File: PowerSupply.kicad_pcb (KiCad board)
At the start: 2 copper layers, 25 x 12.4 mm, 7 parts, among them P1 USB_OTG, P2 CONN_01X03, U1 LM3671MF-3.3

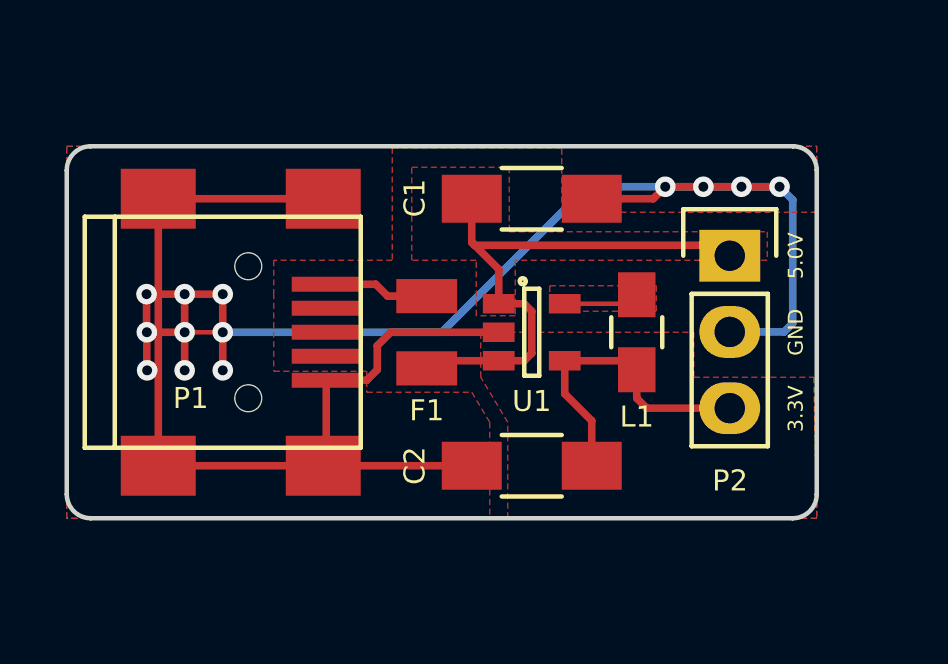
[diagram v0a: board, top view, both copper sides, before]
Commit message: Added MicroSD card adapter
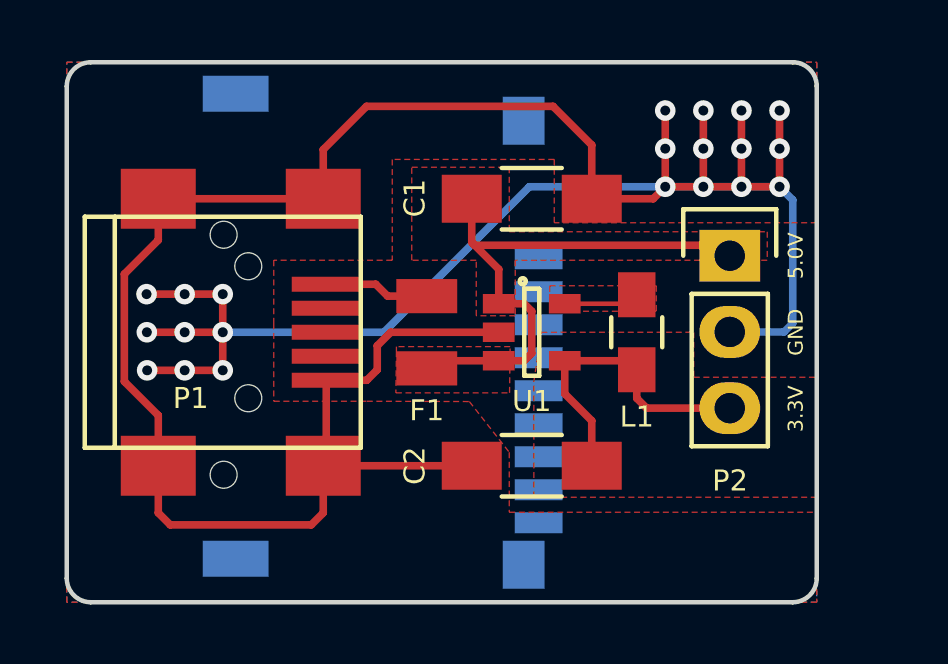
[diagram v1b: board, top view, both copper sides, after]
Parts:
- added U$3: MICRO-SD, PowerSupply:MICRO-SD, B.Cu at (55.2, 156.0)
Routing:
- net GND: track 82.1 -> 106.8 mm, vias 13 -> 21
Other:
- board size 25 x 12.4 mm -> 25 x 18 mm

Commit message: Adds Power-on LED
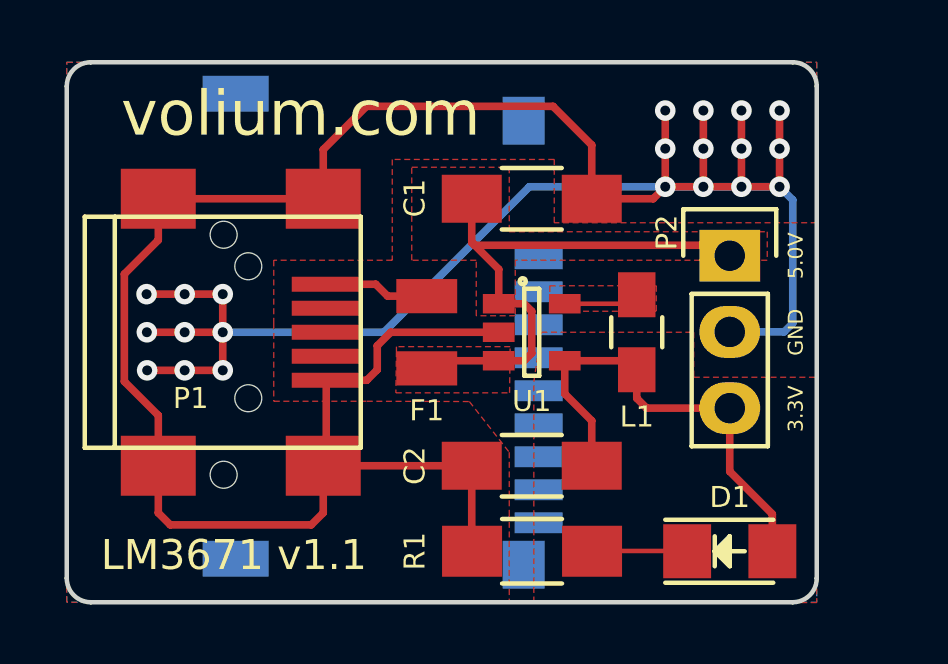
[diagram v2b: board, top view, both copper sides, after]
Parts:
- added D1: LED, LEDs:LED_1206, F.Cu at (72.1, 163.5)
- added R1: R, Resistors_SMD:R_1206_HandSoldering, F.Cu at (65.5, 163.5)
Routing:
- net +3V3: track 10.6 -> 15.9 mm
- net Net-(D1-Pad1): track 0.00 -> 3.17 mm
- net GND: track 106.8 -> 109.7 mm
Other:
- board text added: "LM3671 v1.1"
- board text added: "volium.com"
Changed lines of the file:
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@@
 (kicad_pcb (version 4) (host pcbnew 4.0.3-stable)
   (general
-    (links 17)
+    (links 20)
     (no_connects 0)
     (area 49.924999 147.124999 75.075001 165.275001)
     (thickness 1.6)
-    (drawings 11)
-    (tracks 103)
+    (drawings 13)
+    (tracks 110)
     (zones 0)
-    (modules 8)
-    (nets 9)
+    (modules 10)
+    (nets 10)
   )
   (page A4)
@@
     (0 F.Cu signal)
     (31 B.Cu signal)
-    (34 B.Paste user)
+    (34 B.Paste user hide)
     (35 F.Paste user)
-    (36 B.SilkS user)
+    (36 B.SilkS user hide)
     (37 F.SilkS user)
-    (38 B.Mask user)
+    (38 B.Mask user hide)
     (39 F.Mask user)
     (44 Edge.Cuts user)
@@
   (net 7 "Net-(P1-Pad4)")
   (net 8 "Net-(F1-Pad1)")
+  (net 9 "Net-(D1-Pad1)")
   (net_class Default "This is the default net class."
     (clearance 0.1524)
@@
     (uvia_dia 0.762)
     (uvia_drill 0.508)
+    (add_net "Net-(D1-Pad1)")
     (add_net "Net-(L1-Pad1)")
     (add_net "Net-(P1-Pad2)")
@@
     (descr "Through hole pin header")
     (tags "pin header")
-    (fp_text reference P2 (at 0.01 7.5) (layer F.SilkS)
+    (fp_text reference P2 (at -2.1 -0.78 90) (layer F.SilkS)
       (effects (font (size 0.7 0.7) (thickness 0.15)))
     )
@@
     (pad CD smd rect (at -6.55 10.5 90) (size 0.7 1.6) (layers B.Cu B.Paste B.Mask))
   )
+  (module LEDs:LED_1206 (layer F.Cu)
+    (at 72.1 163.5)
+    (descr "LED 1206 smd package")
+    (tags "LED1206 SMD")
+    (attr smd)
+    (fp_text reference D1 (at 0 -1.8) (layer F.SilkS)
+      (effects (font (size 0.7 0.7) (thickness 0.15)))
+    )
+    (fp_text value LED (at 0 2) (layer F.Fab)
+      (effects (font (size 1 1) (thickness 0.15)))
+    )
+    (fp_line (start -0.5 -0.5) (end -0.5 0.5) (layer F.Fab) (width 0.15))
+    (fp_line (start -0.5 0) (end 0 -0.5) (layer F.Fab) (width 0.15))
+    (fp_line (start 0 0.5) (end -0.5 0) (layer F.Fab) (width 0.15))
+    (fp_line (start 0 -0.5) (end 0 0.5) (layer F.Fab) (width 0.15))
+    (fp_line (start -1.6 0.8) (end -1.6 -0.8) (layer F.Fab) (width 0.15))
+    (fp_line (start 1.6 0.8) (end -1.6 0.8) (layer F.Fab) (width 0.15))
+    (fp_line (start 1.6 -0.8) (end 1.6 0.8) (layer F.Fab) (width 0.15))
+    (fp_line (start -1.6 -0.8) (end 1.6 -0.8) (layer F.Fab) (width 0.15))
+    (fp_line (start -2.15 1.05) (end 1.45 1.05) (layer F.SilkS) (width 0.15))
+    (fp_line (start -2.15 -1.05) (end 1.45 -1.05) (layer F.SilkS) (width 0.15))
+    (fp_line (start -0.1 -0.3) (end -0.1 0.3) (layer F.SilkS) (width 0.15))
+    (fp_line (start -0.1 0.3) (end -0.4 0) (layer F.SilkS) (width 0.15))
+    (fp_line (start -0.4 0) (end -0.2 -0.2) (layer F.SilkS) (width 0.15))
+    (fp_line (start -0.2 -0.2) (end -0.2 0.05) (layer F.SilkS) (width 0.15))
+    (fp_line (start -0.2 0.05) (end -0.25 0) (layer F.SilkS) (width 0.15))
+    (fp_line (start -0.5 -0.5) (end -0.5 0.5) (layer F.SilkS) (width 0.15))
+    (fp_line (start 0 0) (end 0.5 0) (layer F.SilkS) (width 0.15))
+    (fp_line (start -0.5 0) (end 0 -0.5) (layer F.SilkS) (width 0.15))
+    (fp_line (start 0 -0.5) (end 0 0.5) (layer F.SilkS) (width 0.15))
+    (fp_line (start 0 0.5) (end -0.5 0) (layer F.SilkS) (width 0.15))
+    (fp_line (start 2.5 -1.25) (end -2.5 -1.25) (layer F.CrtYd) (width 0.05))
+    (fp_line (start -2.5 -1.25) (end -2.5 1.25) (layer F.CrtYd) (width 0.05))
+    (fp_line (start -2.5 1.25) (end 2.5 1.25) (layer F.CrtYd) (width 0.05))
+    (fp_line (start 2.5 1.25) (end 2.5 -1.25) (layer F.CrtYd) (width 0.05))
+    (pad 2 smd rect (at 1.41986 0 180) (size 1.59766 1.80086) (layers F.Cu F.Paste F.Mask)
+      (net 3 +3V3))
+    (pad 1 smd rect (at -1.41986 0 180) (size 1.59766 1.80086) (layers F.Cu F.Paste F.Mask)
+      (net 9 "Net-(D1-Pad1)"))
+    (model LEDs.3dshapes/LED_1206.wrl
+      (at (xyz 0 0 0))
+      (scale (xyz 1 1 1))
+      (rotate (xyz 0 0 180))
+    )
+  )
+  (module Resistors_SMD:R_1206_HandSoldering (layer F.Cu)
+    (at 65.51 163.5 180)
+    (descr "Resistor SMD 1206, hand soldering")
+    (tags "resistor 1206")
+    (attr smd)
+    (fp_text reference R1 (at 3.91 0 270) (layer F.SilkS)
+      (effects (font (size 0.7 0.7) (thickness 0.15)))
+    )
+    (fp_text value R (at 0 2.3 180) (layer F.Fab)
+      (effects (font (size 1 1) (thickness 0.15)))
+    )
+    (fp_line (start -3.3 -1.2) (end 3.3 -1.2) (layer F.CrtYd) (width 0.05))
+    (fp_line (start -3.3 1.2) (end 3.3 1.2) (layer F.CrtYd) (width 0.05))
+    (fp_line (start -3.3 -1.2) (end -3.3 1.2) (layer F.CrtYd) (width 0.05))
+    (fp_line (start 3.3 -1.2) (end 3.3 1.2) (layer F.CrtYd) (width 0.05))
+    (fp_line (start 1 1.075) (end -1 1.075) (layer F.SilkS) (width 0.15))
+    (fp_line (start -1 -1.075) (end 1 -1.075) (layer F.SilkS) (width 0.15))
+    (pad 1 smd rect (at -2 0 180) (size 2 1.7) (layers F.Cu F.Paste F.Mask)
+      (net 9 "Net-(D1-Pad1)"))
+    (pad 2 smd rect (at 2 0 180) (size 2 1.7) (layers F.Cu F.Paste F.Mask)
+      (net 2 GND))
+    (model Resistors_SMD.3dshapes/R_1206_HandSoldering.wrl
+      (at (xyz 0 0 0))
+      (scale (xyz 1 1 1))
+      (rotate (xyz 0 0 0))
+    )
+  )
+  (gr_text "LM3671 v1.1" (at 55.57 163.63) (layer F.SilkS)
+    (effects (font (size 1 1) (thickness 0.1)))
+  )
+  (gr_text volium.com (at 57.8 148.92) (layer F.SilkS)
+    (effects (font (size 1.5 1.5) (thickness 0.2)))
+  )
   (gr_text 5.0V (at 74.3 153.65 90) (layer F.SilkS)
     (effects (font (size 0.5 0.5) (thickness 0.1)))
@@
   (segment (start 62 157.40396) (end 62.25396 157.15) (width 0.254) (layer F.Cu) (net 1))
   (segment (start 62.25396 157.15) (end 64.4 157.15) (width 0.254) (layer F.Cu) (net 1))
+  (segment (start 63.5 160.65) (end 63.5 163.48) (width 0.254) (layer F.Cu) (net 2))
+  (segment (start 63.5 163.48) (end 63.51 163.49) (width 0.254) (layer F.Cu) (net 2))
   (segment (start 67.5 151.75) (end 67.5 149.96) (width 0.254) (layer F.Cu) (net 2))
   (segment (start 58.55026 150.10974) (end 58.55026 151.74992) (width 0.254) (layer F.Cu) (net 2))
@@
   (segment (start 58.55026 160.65008) (end 63.49992 160.65008) (width 0.254) (layer F.Cu) (net 2))
   (segment (start 63.49992 160.65008) (end 63.5 160.65) (width 0.254) (layer F.Cu) (net 2))
+  (segment (start 73.51986 163.5) (end 73.51986 162.25986) (width 0.254) (layer F.Cu) (net 3) (status 400000))
+  (segment (start 72.1 160.84) (end 72.1 158.73) (width 0.254) (layer F.Cu) (net 3) (status 800000))
+  (segment (start 73.51986 162.25986) (end 72.1 160.84) (width 0.254) (layer F.Cu) (net 3))
   (segment (start 69 157.45) (end 69 158.4) (width 0.254) (layer F.Cu) (net 3))
   (segment (start 69.33 158.73) (end 72.1 158.73) (width 0.254) (layer F.Cu) (net 3))
@@
   (segment (start 60.69604 154.99604) (end 60.2998 154.5998) (width 0.254) (layer F.Cu) (net 8))
   (segment (start 60.2998 154.5998) (end 58.64932 154.5998) (width 0.254) (layer F.Cu) (net 8))
+  (segment (start 67.51 163.49) (end 70.67014 163.49) (width 0.1524) (layer F.Cu) (net 9))
+  (segment (start 70.67014 163.49) (end 70.68014 163.5) (width 0.1524) (layer F.Cu) (net 9))
   (zone (net 3) (net_name +3V3) (layer F.Cu) (hatch edge 0.508)
     (connect_pads (clearance 0.254))
@@
     (polygon
       (pts
-        (xy 70.9 157.7) (xy 75 157.7) (xy 75 161.7) (xy 65.57 161.7) (xy 65.57 157.84)
+        (xy 70.9 157.7) (xy 75 157.7) (xy 75 165.21) (xy 65.57 165.21) (xy 65.57 157.84)
         (xy 65.82 156.2) (xy 70.9 156.2)
       )
@@
         (xy 75 152.55) (xy 74.1 152.55) (xy 66.25 152.55) (xy 66.25 150.44) (xy 60.85 150.44)
         (xy 60.85 153.8) (xy 56.9 153.8) (xy 56.9 155.9) (xy 56.9 158.5) (xy 60 158.5)
-        (xy 63.42 158.51) (xy 64.75 160.2) (xy 64.75 162.2) (xy 75 162.2) (xy 75 165.2)
-        (xy 50 165.2) (xy 50 147.2) (xy 75 147.2)
+        (xy 63.42 158.51) (xy 64.75 160.2) (xy 64.75 162.2) (xy 64.75 165.2) (xy 50 165.2)
+        (xy 50 147.2) (xy 75 147.2)
       )
     )

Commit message: Changes L1 with 1008 package
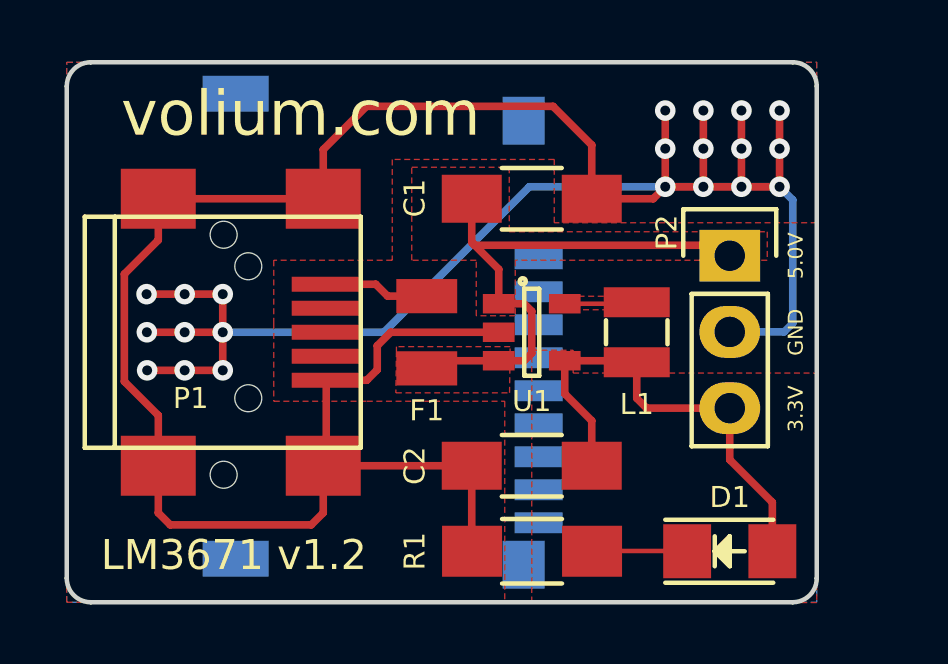
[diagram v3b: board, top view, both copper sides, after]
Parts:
- L1: footprint Capacitors_SMD:C_0805_HandSoldering -> PowerSupply:C_1008_HandSoldering
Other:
- board text added: "LM3671 v1.2"
- board text removed: "LM3671 v1.1"

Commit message: A lot of changes (BOM, layout, routing) Replaces inductor with footprint compatible with CDRH2D09 (Sumida) and NRH2412T (Taiyo Yuden) Removes access to 5V pin (replaced 3-pin connector with 2-pin) Updated layout, now more closely matching Adafruit's version of LM3671 breakout board, and following TI's layout example.
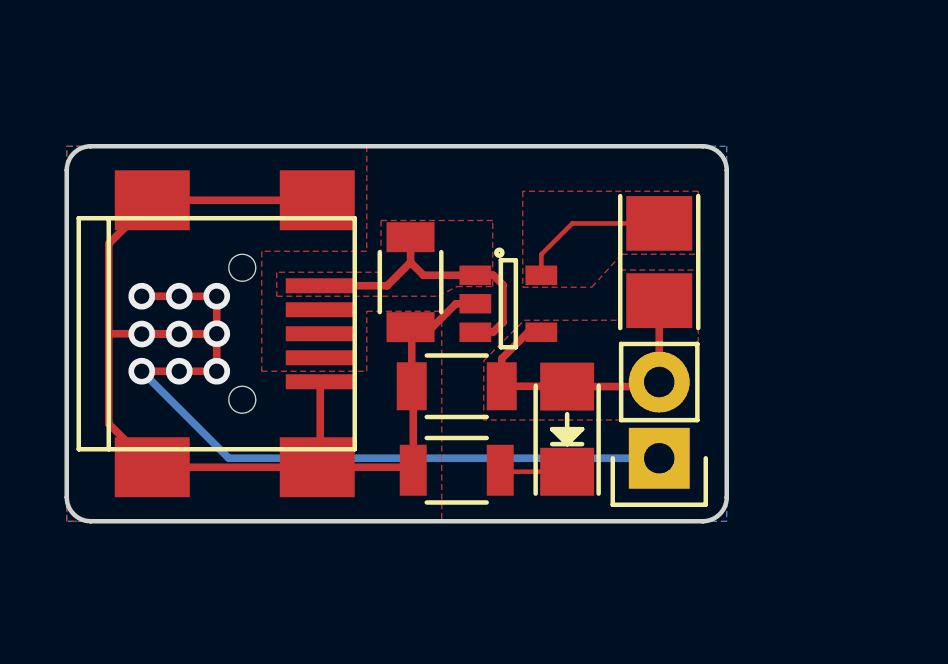
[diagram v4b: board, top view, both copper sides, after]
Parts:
- removed F1: FUSE, Fuse_Holders_and_Fuses:Fuse_SMD1206_Reflow
- removed U$3: MICRO-SD, PowerSupply:MICRO-SD
- C1, C2: footprint Capacitors_SMD:C_1206_HandSoldering -> Capacitors_SMD:C_1206
- L1: footprint PowerSupply:C_1008_HandSoldering -> Inductors:Inductor_Taiyo-Yuden_NR-24xx_HandSoldering
- P2: footprint Pin_Headers:Pin_Header_Straight_1x03 -> Pin_Headers:Pin_Header_Straight_1x02
- R1: footprint Resistors_SMD:R_1206_HandSoldering -> Resistors_SMD:R_1206
- moved P2 7.15 mm to (69.8, 160.4), turned to 180 degrees
- moved D1 6.78 mm to (66.7, 159.4), turned to 90 degrees
- moved C1 4.90 mm to (61.5, 154.5), turned to 270 degrees
- moved R1 3.69 mm to (63.0, 160.8)
- moved C2 3.64 mm to (63.0, 158.0)
- moved L1 2.46 mm to (69.8, 153.9)
- moved U1 1.23 mm to (64.7, 155.2)
- moved P1 0.21 mm to (55.0, 156.2)
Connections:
- P1 pad 1: Net-(F1-Pad1) -> VCC
- P1 pad 2: Net-(P1-Pad2) -> (no net)
- P1 pad 3: Net-(P1-Pad3) -> (no net)
- P1 pad 4: Net-(P1-Pad4) -> (no net)
- P2 pad 1: VCC -> GND
- P2 pad 2: GND -> +3V3
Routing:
- net GND: track 109.7 -> 66.6 mm, vias 21 -> 9
- net VCC: track 19.0 -> 9.88 mm
- net +3V3: track 15.9 -> 10.6 mm
- net Net-(F1-Pad1): track 3.51 -> 0.00 mm
- net Net-(L1-Pad1): track 2.52 -> 5.05 mm
- net Net-(D1-Pad1): track 3.17 -> 2.25 mm
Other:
- board size 25 x 18 mm -> 22 x 12.5 mm
- net class Power: via_dia 0.6858 -> 0.889; via_drill 0.3302 -> 0.508
- board text added: "LM3671 v1.3"
- board text removed: "3.3V"
- board text removed: "5.0V"
- board text removed: "GND"
- board text removed: "LM3671 v1.2"
